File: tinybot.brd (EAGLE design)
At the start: 34.6 x 48.3 mm, 18 parts, among them Q1 MOSFET-PCHANNEL, Q2 2N7002PW, Q3 2N7002PW, U1 MCP73831, U2 TINY85-20-DIP

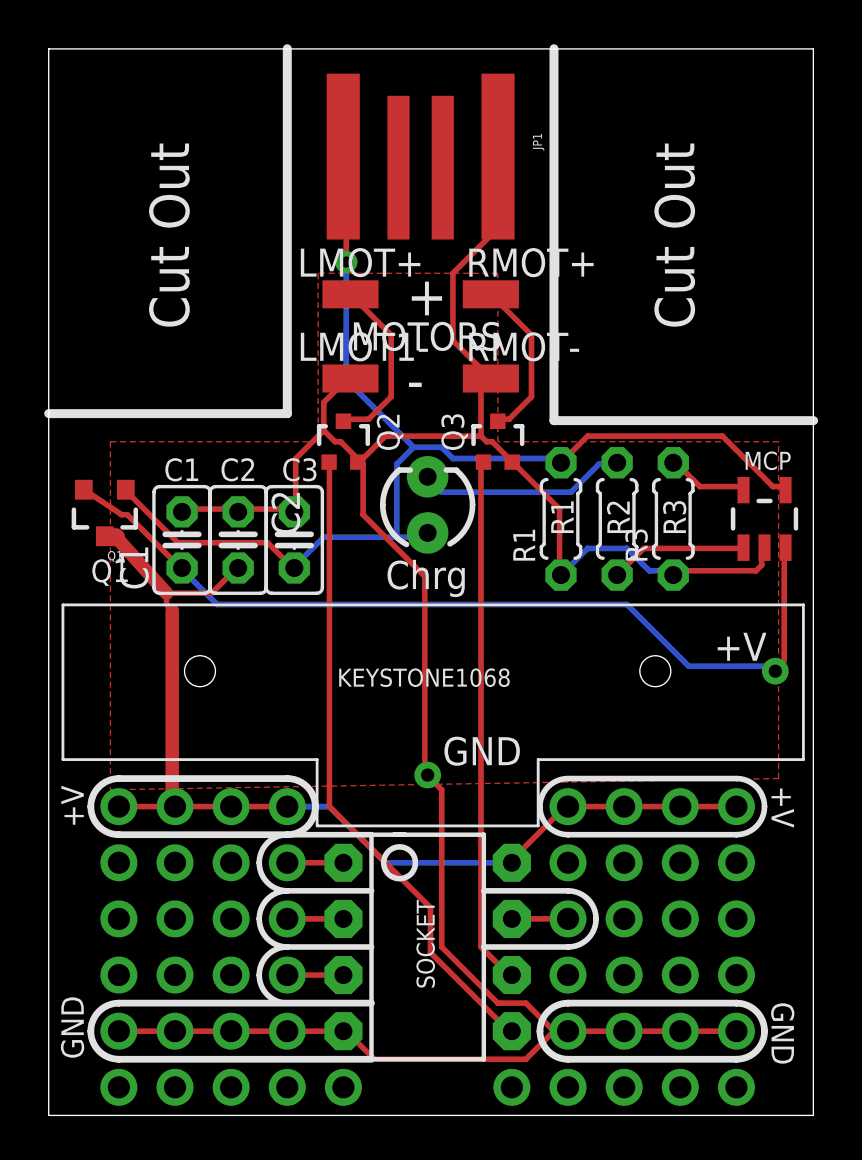
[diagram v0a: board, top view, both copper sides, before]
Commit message: update milling layer with board outline
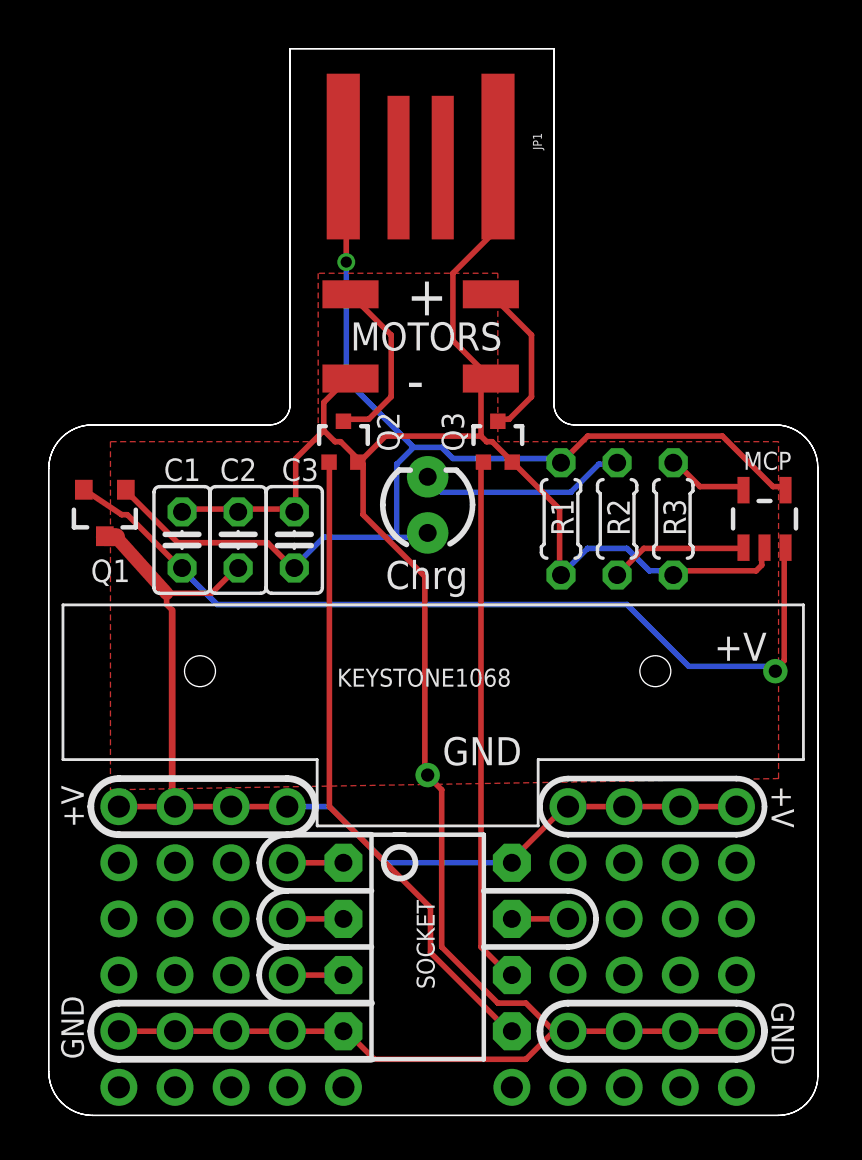
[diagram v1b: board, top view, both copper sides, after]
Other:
- board size 34.6 x 48.3 mm -> 34.8 x 48.3 mm
- board text removed: "Cut Out"

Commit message: fixed mosfet wiring error
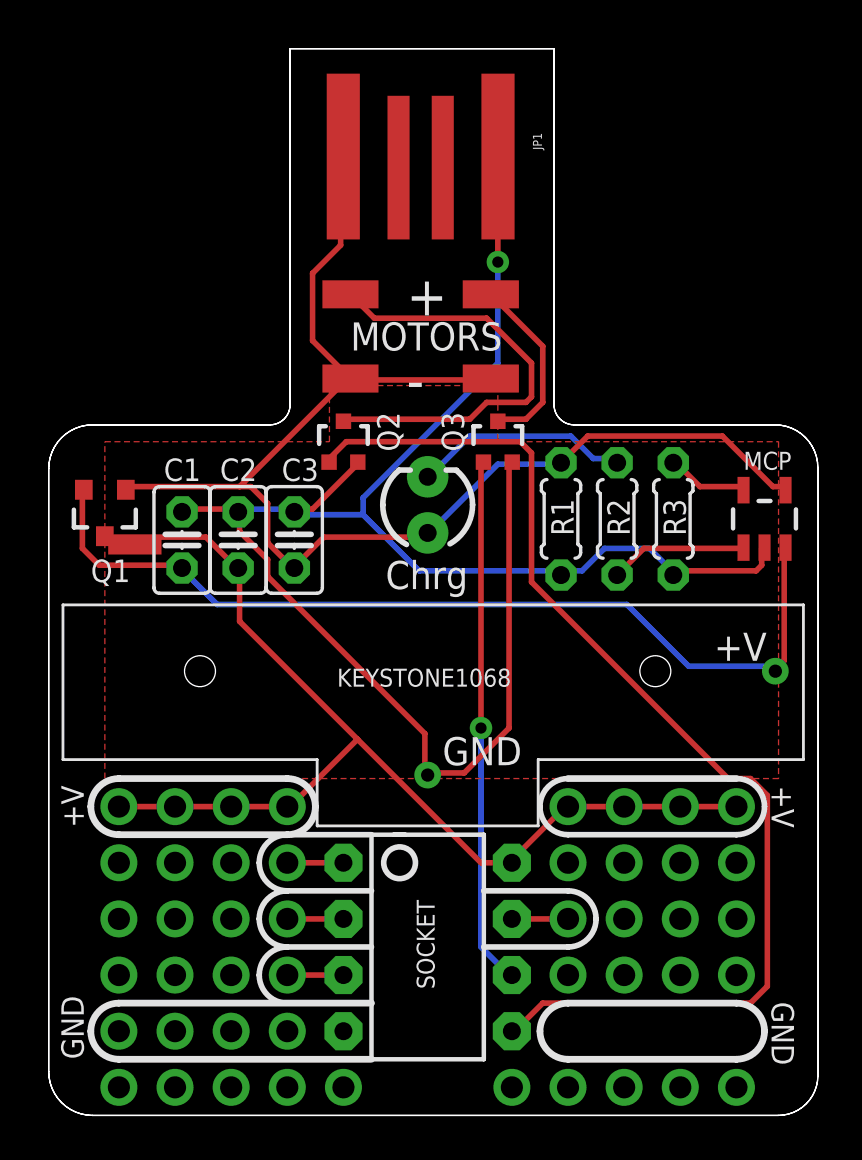
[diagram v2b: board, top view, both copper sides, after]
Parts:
- moved RMOT+ 3.81 mm to (20.0, 33.3)
- moved RMOT- 3.81 mm to (20.0, 37.1)
- renumbered LMOT+ to LMOT-, LMOT1- to LMOT1+
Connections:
- net 5V: now also LMOT1+.1, RMOT+.1
- net GND: no longer LMOT1+.1, RMOT-.1
- net N$8: now also RMOT-.1; no longer RMOT+.1
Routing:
- net GND: track 113.6 -> 84.6 mm, vias 8 -> 5
- net N$4: track 29.2 -> 51.4 mm
- net N$6: track 8.01 -> 20.0 mm
- net 5V: track 53.4 -> 60.8 mm, vias 1 -> 0
- net VBAT: track 40.4 -> 42.2 mm
- net VCC: track 47.7 -> 49.3 mm
- net N$8: track 7.43 -> 8.30 mm
- net N$5: vias 0 -> 1

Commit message: fixed motor mosfet wiring (again)
Still had it wrong!  Motor mosfets connected to 5V (from USB), not VCC.
Now fixed.

Also added logo/name/url to bottom silk!
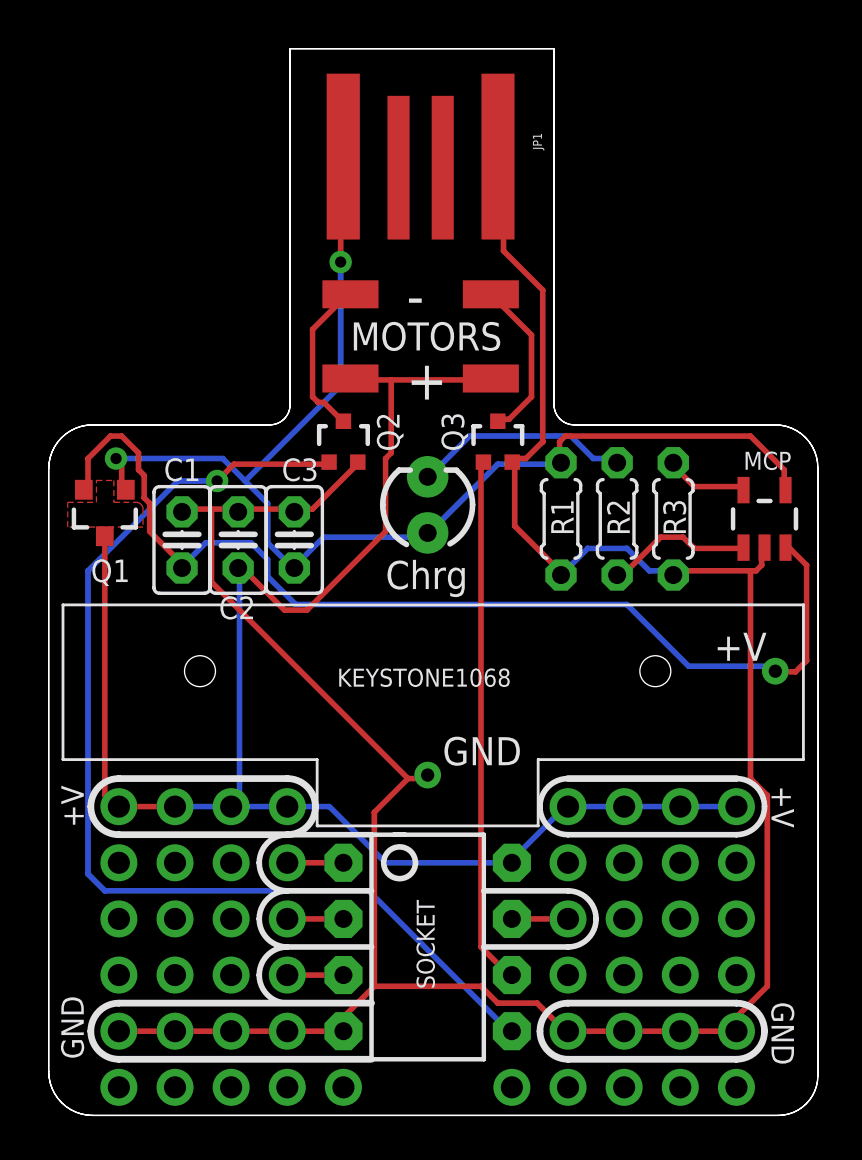
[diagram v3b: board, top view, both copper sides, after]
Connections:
- net 5V: no longer LMOT1+.1, RMOT+.1
- net VCC: now also LMOT1+.1, RMOT+.1
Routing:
- net GND: track 84.6 -> 120.7 mm, vias 5 -> 8
- net VCC: track 49.3 -> 76.1 mm
- net N$6: track 20.0 -> 7.25 mm
- net VBAT: track 42.2 -> 48.1 mm
- net 5V: track 60.8 -> 56.1 mm, vias 0 -> 2
- net N$4: track 51.4 -> 48.8 mm, vias 0 -> 1
- net N$8: track 8.30 -> 7.43 mm
- net N$5: vias 1 -> 0
- added copper zone on layer 1, net VCC
- removed copper zone on layer 1, net GND
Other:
- board text added: "TinyBot"
- board text added: "hackaday.io/project/2054"
- board text added: "version 0.1 7/24/14"

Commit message: Decreased charge current from 500mA to 100mA
R3 changed from 2K to 10K
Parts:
- R3: value 2K -> 10K
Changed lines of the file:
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@@
 </element>
 <element name="R1" library="rcl" package="0204/5" value="100K" x="23.1775" y="26.9875" smashed="yes" rot="R90"/>
-<element name="R3" library="rcl" package="0204/5" value="2K" x="28.2575" y="26.9875" smashed="yes" rot="R90"/>
+<element name="R3" library="rcl" package="0204/5" value="10K" x="28.2575" y="26.9875" smashed="yes" rot="R90"/>
 <element name="C1" library="rcl" package="C025-025X050" value="4.7 uf" x="6.0325" y="26.035" smashed="yes" rot="R90"/>
 <element name="C2" library="rcl" package="C025-025X050" value="1 uf" x="8.5725" y="26.035" smashed="yes" rot="R270"/>

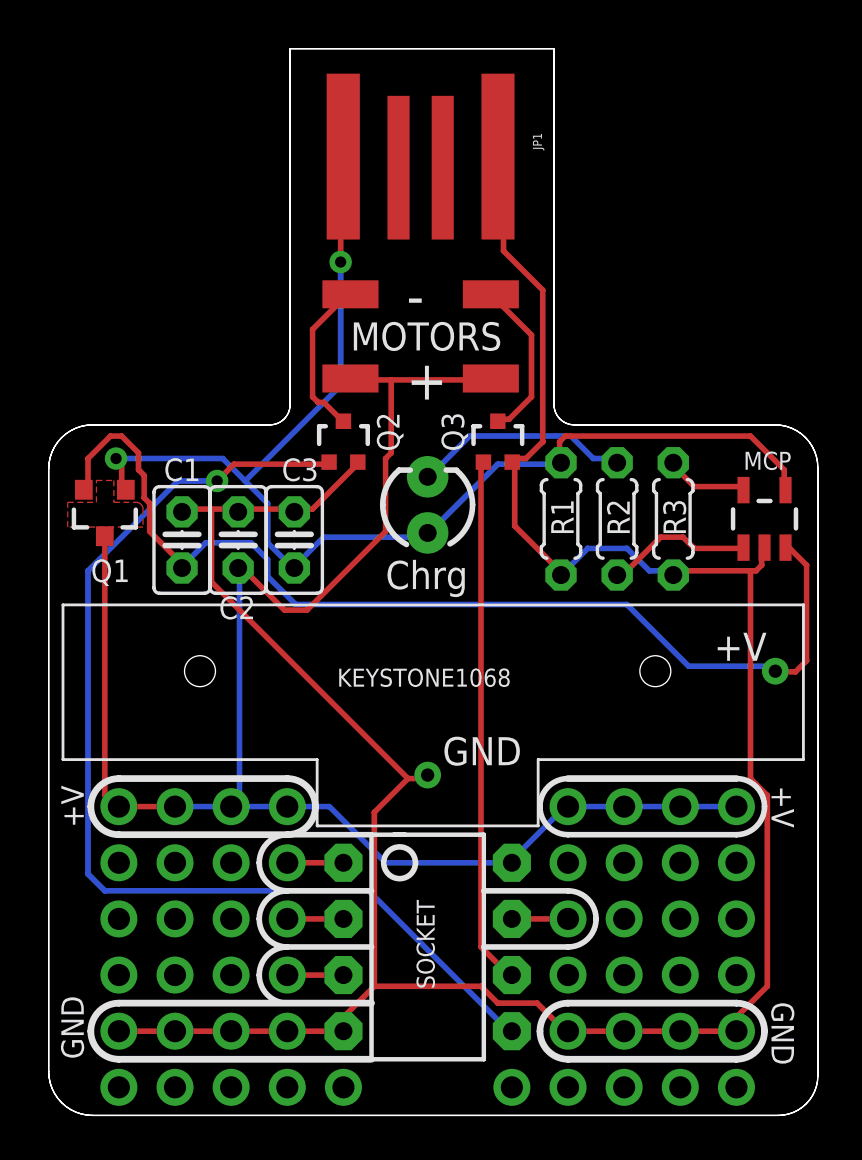
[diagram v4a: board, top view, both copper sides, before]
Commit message: improved mosfet pad layout and corrected battery holder hole size
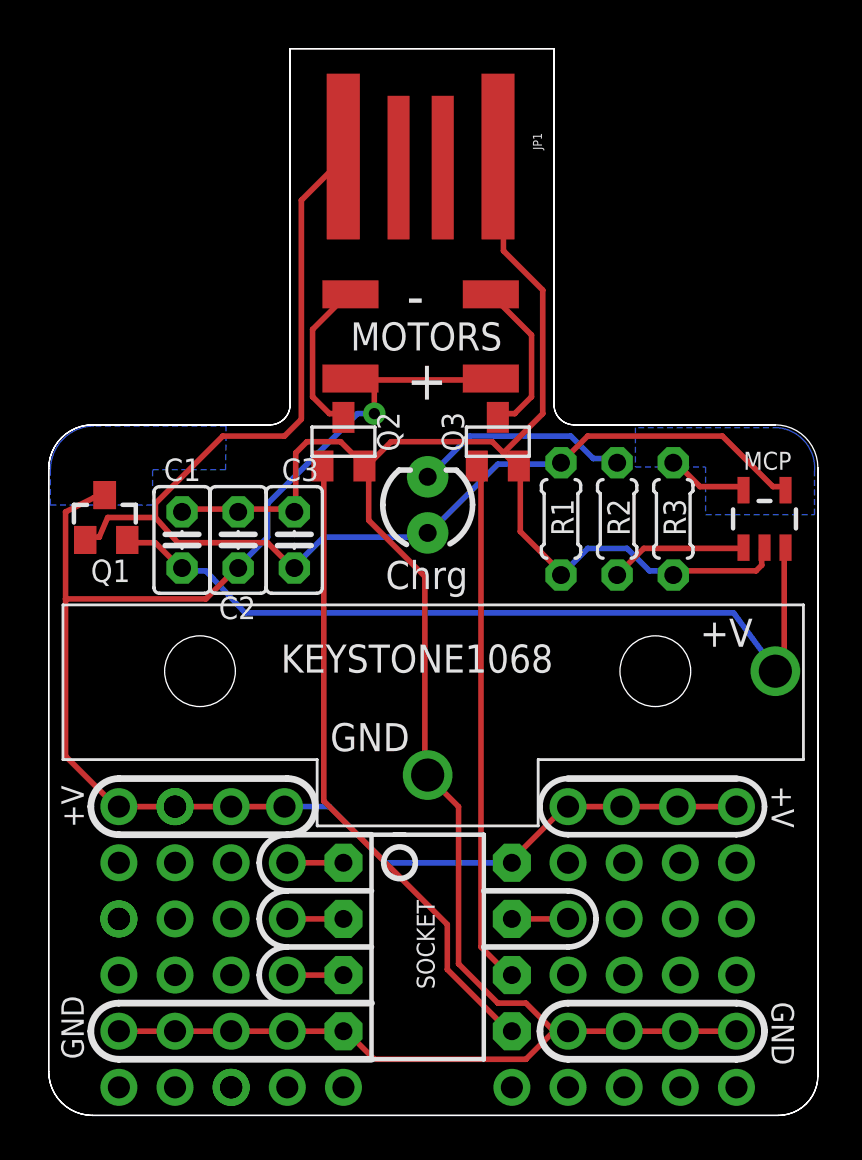
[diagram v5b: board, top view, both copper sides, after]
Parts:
- Q2, Q3: device SparkFun-DiscreteSemi:SOT323 -> SparkFun-DiscreteSemi:SOT23
- moved Q1 0.38 mm to (2.54, 26.9), turned to 0 degrees
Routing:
- net N$4: track 48.8 -> 29.2 mm, vias 1 -> 0
- net GND: track 120.7 -> 110.5 mm
- net VBAT: track 48.1 -> 37.9 mm
- net 5V: track 56.1 -> 58.5 mm, vias 2 -> 0
- net VCC: track 76.1 -> 74.1 mm, vias 8 -> 10
- added copper zone on layer 16, net N$22
- added copper zone on layer 16, net N$25
- removed copper zone on layer 1, net VCC
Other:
- board text added: "version 0.2 12/01/14"
- board text removed: "version 0.1 7/24/14"
